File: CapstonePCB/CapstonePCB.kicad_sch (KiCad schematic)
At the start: 30 parts, among them J1 Conn_02x40_Counter_Clockwise, J2 Barrel_Jack, SW1 SW_Push, U1 NUCLEO64-F411RE, U2 LP-MSPM0G3507, U3 STSPIN220, U4 SN74AHC14N, U5 LM7805_TO220, U6 TLV1117-33, U8 APDS-9306

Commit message: Updated routing for PCB
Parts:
- added C2, C3: 0.47 uF, Capacitor_SMD:C_0201_0603Metric, symbol Device:C
- added D2: LED, LED_THT:LED_D3.0mm_FlatTop, symbol Device:LED
- added PullUpResistor2, PullUpResistor3, PullUpResistor4, R2, R3: 10 kOhm, Resistor_SMD:R_0201_0603Metric, symbol Device:R
- added R_STBY2: 5.5k ohm, Resistor_SMD:R_0201_0603Metric, symbol Device:R
- added SW2, SW3: SW_Push, Button_Switch_THT:SW_PUSH_6mm_H7.3mm, symbol Switch:SW_Push
- added U7: COM-09032, Joystick:XDCR_COM-09032, symbol COM-09032:COM-09032
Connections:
- net +12V: now also R_STBY2.1
- net +5V: now also PullUpResistor2.2, PullUpResistor3.2, PullUpResistor4.2
- net GNDREF: now also C1.1, J1.27 (Pin_27), J1.28 (Pin_28), U3.11 (REF), C2.2, C3.2, D2.1 (K), SW2.1, SW3.1, U7.B2A (SEL-), U7.H3 (H-), U7.S1 (SHIELD), U7.S2 (SHIELD), U7.S3 (SHIELD), U7.S4 (SHIELD), U7.V3 (V-); no longer C1.2
- net VDD: now also U7.H1 (H+), U7.V1 (V+)
- net at U3.1 (DIR): now also J1.35 (Pin_35), J1.36 (Pin_36)
- net at U3.15 (MODE2): now also J1.29 (Pin_29), J1.30 (Pin_30)
- net at U3.16 (MODE1): now also J1.31 (Pin_31), J1.32 (Pin_32)
- net at U3.2 (STCK): now also J1.33 (Pin_33), J1.34 (Pin_34)
- net at U3.3 (OUTA1): now also J1.37 (Pin_37), J1.38 (Pin_38)
- net at U3.5 (OUTA2): now also J1.39 (Pin_39), J1.40 (Pin_40)
- net at R1.1, U4.1 (1A): now also C1.2; no longer C1.1
- net at J1.41 (Pin_41), J1.42 (Pin_42): no longer U4.2 (1Y)
- net at U4.3 (2A): now also C2.1, R2.1
- net at U4.4 (2Y): now also J1.3 (Pin_3), J1.4 (Pin_4)
- net at U4.5 (3A): now also C3.1, R3.1
- net at U4.6 (3Y): now also J1.5 (Pin_5), J1.6 (Pin_6)
- net at J1.1 (Pin_1), J1.2 (Pin_2): now also U4.2 (1Y)
- net at J1.21 (Pin_21), J1.22 (Pin_22): now also U7.H2 (H)
- net at J1.23 (Pin_23), J1.24 (Pin_24): now also U7.V2 (V)
- net Button No Debouning: now reaches J1.67 (Pin_67), J1.68 (Pin_68)
- net Button No Debouning: now also PullUpResistor2.1, SW2.2
- net Button Input renamed Button1 Input
- new net: PullUpResistor4.1, R3.2, U7.B1A (SEL+)
- new net: D2.2 (A), R_STBY2.2
- new net Button2 Input: PullUpResistor3.1, R2.2, SW3.2
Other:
- moved on the sheet: C1, C_EN1, C_EN2, C_SPOIL1, C_STBY1, C_s1, D1, J1, PullUpResistor1, R1, R_COFF1, R_COFF2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

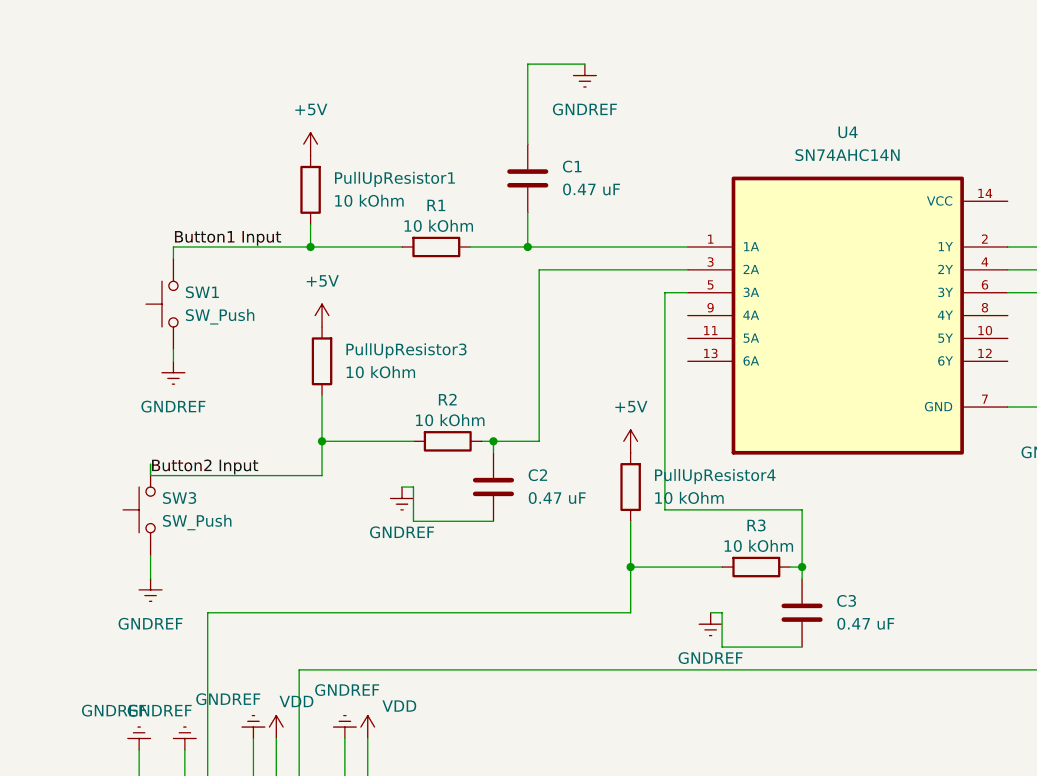
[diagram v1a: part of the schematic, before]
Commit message: Updated button routing
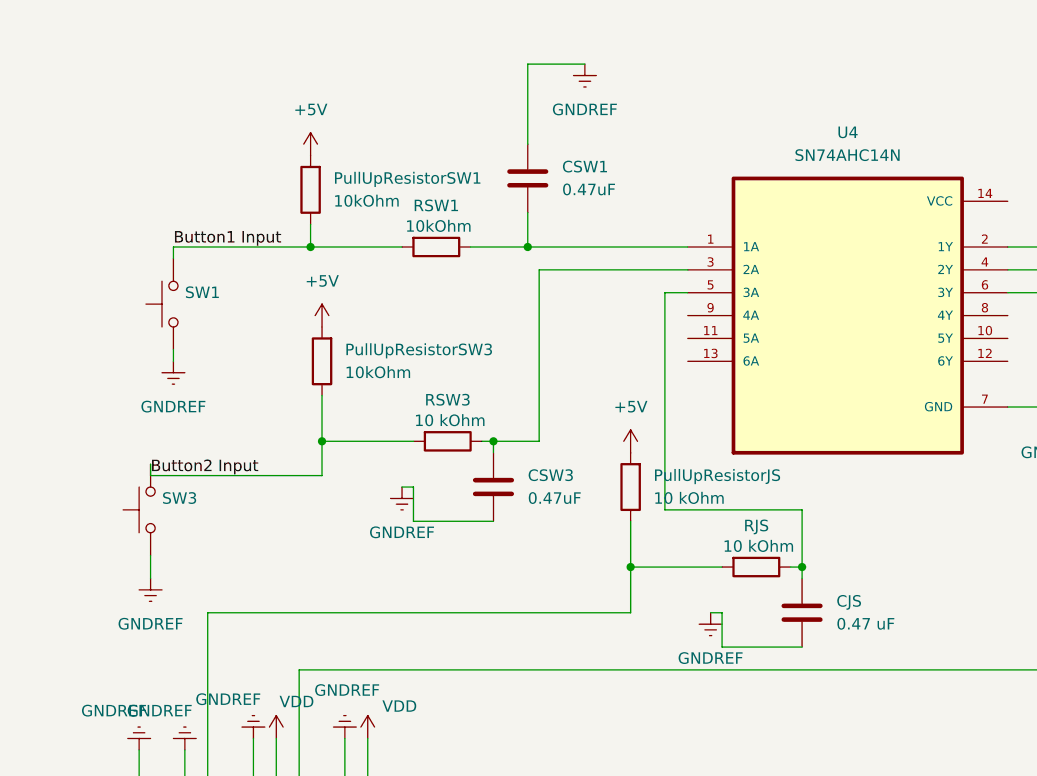
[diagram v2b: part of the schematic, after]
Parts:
- CSW1: renamed from C1; value 0.47 uF -> 0.47uF
- CSW3: renamed from C2; value 0.47 uF -> 0.47uF
- PullUpResistorSW1: renamed from PullUpResistor1; value 10 kOhm -> 10kOhm
- PullUpResistorSW3: renamed from PullUpResistor3; value 10 kOhm -> 10kOhm
- RSW1: renamed from R1; value 10 kOhm -> 10kOhm
- renumbered C3 to CJS, PullUpResistor4 to PullUpResistorJS, R3 to RJS, R2 to RSW3
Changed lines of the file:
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@@
 		(on_board yes)
 		(dnp no)
-		(property "Reference" "R2"
+		(property "Reference" "RSW3"
 			(at 194.31 55.118 90)
 			(effects
@@
 			(project "CapstonePCB"
 				(path "/39e7582f-7765-4fc9-b934-76d5b28d9065"
-					(reference "R2")
+					(reference "RSW3")
 					(unit 1)
 				)
@@
 		(dnp no)
 		(fields_autoplaced yes)
-		(property "Reference" "PullUpResistor1"
+		(property "Reference" "PullUpResistorSW1"
 			(at 181.61 30.4799 0)
 			(effects
@@
 			)
 		)
-		(property "Value" "10 kOhm"
+		(property "Value" "10kOhm"
 			(at 181.61 33.0199 0)
 			(effects
@@
 			(project "CapstonePCB"
 				(path "/39e7582f-7765-4fc9-b934-76d5b28d9065"
-					(reference "PullUpResistor1")
+					(reference "PullUpResistorSW1")
 					(unit 1)
 				)
@@
 		(dnp no)
 		(fields_autoplaced yes)
-		(property "Reference" "C2"
+		(property "Reference" "CSW3"
 			(at 203.2 63.4999 0)
 			(effects
@@
 			)
 		)
-		(property "Value" "0.47 uF"
+		(property "Value" "0.47uF"
 			(at 203.2 66.0399 0)
 			(effects
@@
 			(project "CapstonePCB"
 				(path "/39e7582f-7765-4fc9-b934-76d5b28d9065"
-					(reference "C2")
+					(reference "CSW3")
 					(unit 1)
 				)
@@
 				)
 				(justify right)
+				(hide yes)
 			)
 		)
@@
 		(dnp no)
 		(fields_autoplaced yes)
-		(property "Reference" "C1"
+		(property "Reference" "CSW1"
 			(at 207.01 29.2099 0)
 			(effects
@@
 			)
 		)
-		(property "Value" "0.47 uF"
+		(property "Value" "0.47uF"
 			(at 207.01 31.7499 0)
 			(effects
@@
 			(project ""
 				(path "/39e7582f-7765-4fc9-b934-76d5b28d9065"
-					(reference "C1")
+					(reference "CSW1")
 					(unit 1)
 				)
@@
 		(dnp no)
 		(fields_autoplaced yes)
-		(property "Reference" "PullUpResistor4"
+		(property "Reference" "PullUpResistorJS"
 			(at 217.17 63.4999 0)
 			(effects
@@
 			(project "CapstonePCB"
 				(path "/39e7582f-7765-4fc9-b934-76d5b28d9065"
-					(reference "PullUpResistor4")
+					(reference "PullUpResistorJS")
 					(unit 1)
 				)
@@
 		(on_board yes)
 		(dnp no)
-		(property "Reference" "R3"
+		(property "Reference" "RJS"
 			(at 228.6 69.088 90)
 			(effects
@@
 			(project "CapstonePCB"
 				(path "/39e7582f-7765-4fc9-b934-76d5b28d9065"
-					(reference "R3")
+					(reference "RJS")
 					(unit 1)
 				)
@@
 		(dnp no)
 		(fields_autoplaced yes)
-		(property "Reference" "PullUpResistor3"
+		(property "Reference" "PullUpResistorSW3"
 			(at 182.88 49.5299 0)
 			(effects
@@
 			)
 		)
-		(property "Value" "10 kOhm"
+		(property "Value" "10kOhm"
 			(at 182.88 52.0699 0)
 			(effects
@@
 			(project "CapstonePCB"
 				(path "/39e7582f-7765-4fc9-b934-76d5b28d9065"
-					(reference "PullUpResistor3")
+					(reference "PullUpResistorSW3")
 					(unit 1)
 				)
@@
 		(dnp no)
 		(fields_autoplaced yes)
-		(property "Reference" "C3"
+		(property "Reference" "CJS"
 			(at 237.49 77.4699 0)
 			(effects
@@
 			(project "CapstonePCB"
 				(path "/39e7582f-7765-4fc9-b934-76d5b28d9065"
-					(reference "C3")
+					(reference "CJS")
 					(unit 1)
 				)
@@
 				)
 				(justify right)
+				(hide yes)
 			)
 		)
@@
 		(on_board yes)
 		(dnp no)
-		(property "Reference" "R1"
+		(property "Reference" "RSW1"
 			(at 193.04 33.528 90)
 			(effects
@@
 			)
 		)
-		(property "Value" "10 kOhm"
+		(property "Value" "10kOhm"
 			(at 193.294 35.814 90)
 			(effects
@@
 			(project ""
 				(path "/39e7582f-7765-4fc9-b934-76d5b28d9065"
-					(reference "R1")
+					(reference "RSW1")
 					(unit 1)
 				)

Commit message: Updated naming on silkscreen
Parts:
- renumbered CJS to CJS1, PullUpResistorJS to PullUpResistorJS1, RJS to RJS1
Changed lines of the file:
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@@
 		(dnp no)
 		(fields_autoplaced yes)
-		(property "Reference" "PullUpResistorJS"
+		(property "Reference" "PullUpResistorJS1"
 			(at 217.17 63.4999 0)
 			(effects
@@
 			(project "CapstonePCB"
 				(path "/39e7582f-7765-4fc9-b934-76d5b28d9065"
-					(reference "PullUpResistorJS")
+					(reference "PullUpResistorJS1")
 					(unit 1)
 				)
@@
 		(on_board yes)
 		(dnp no)
-		(property "Reference" "RJS"
+		(property "Reference" "RJS1"
 			(at 228.6 69.088 90)
 			(effects
@@
 			(project "CapstonePCB"
 				(path "/39e7582f-7765-4fc9-b934-76d5b28d9065"
-					(reference "RJS")
+					(reference "RJS1")
 					(unit 1)
 				)
@@
 		(dnp no)
 		(fields_autoplaced yes)
-		(property "Reference" "CJS"
+		(property "Reference" "CJS1"
 			(at 237.49 77.4699 0)
 			(effects
@@
 			(project "CapstonePCB"
 				(path "/39e7582f-7765-4fc9-b934-76d5b28d9065"
-					(reference "CJS")
-					(unit 1)
-				)
+					(reference "CJS1")
+					(unit 1)
+				)

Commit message: Updated rounting
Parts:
- renumbered C_STBY2 to C_BP1, C_STBY3 to C_BP2, R_STBY2 to R_INDC
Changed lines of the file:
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@@
 		(dnp no)
 		(fields_autoplaced yes)
-		(property "Reference" "R_STBY2"
+		(property "Reference" "R_INDC"
 			(at 31.75 177.7999 0)
 			(effects
@@
 			(project "CapstonePCB"
 				(path "/39e7582f-7765-4fc9-b934-76d5b28d9065"
-					(reference "R_STBY2")
+					(reference "R_INDC")
 					(unit 1)
 				)
@@
 		(dnp no)
 		(fields_autoplaced yes)
-		(property "Reference" "C_STBY3"
+		(property "Reference" "C_BP2"
 			(at 54.61 21.5962 0)
 			(effects
@@
 			(project "CapstonePCB"
 				(path "/39e7582f-7765-4fc9-b934-76d5b28d9065"
-					(reference "C_STBY3")
+					(reference "C_BP2")
 					(unit 1)
 				)
@@
 		(dnp no)
 		(fields_autoplaced yes)
-		(property "Reference" "C_STBY2"
+		(property "Reference" "C_BP1"
 			(at 41.91 21.5962 0)
 			(effects
@@
 			(project "CapstonePCB"
 				(path "/39e7582f-7765-4fc9-b934-76d5b28d9065"
-					(reference "C_STBY2")
+					(reference "C_BP1")
 					(unit 1)
 				)

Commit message: Formatting change
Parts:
- renumbered R_INDC to R_INDC1
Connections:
- net GNDREF: no longer J1.27 (Pin_27), J1.28 (Pin_28), U3.11 (REF)
- net at J1.21 (Pin_21), J1.22 (Pin_22): no longer U7.H2 (H)
- net at J1.23 (Pin_23), J1.24 (Pin_24): no longer U7.V2 (V)
- net at J1.11 (Pin_11), J1.12 (Pin_12): now also U7.H2 (H)
- net at J1.13 (Pin_13), J1.14 (Pin_14): now also U7.V2 (V)
- new net: J1.27 (Pin_27), J1.28 (Pin_28), U3.11 (REF)

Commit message: Changed caps to through-hole
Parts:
- C_EN1, C_EN2, C_SPOIL1, C_STBY1, C_s1: footprint Capacitor_SMD:C_0201_0603Metric -> Capacitor_THT:C_Disc_D4.3mm_W1.9mm_P5.00mm
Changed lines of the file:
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@@
 			)
 		)
-		(property "Footprint" "Capacitor_SMD:C_0201_0603Metric"
+		(property "Footprint" "Capacitor_THT:C_Disc_D4.3mm_W1.9mm_P5.00mm"
 			(at 306.07 147.32 0)
 			(effects
@@
 			)
 		)
-		(property "Footprint" "Capacitor_SMD:C_0201_0603Metric"
+		(property "Footprint" "Capacitor_THT:C_Disc_D4.3mm_W1.9mm_P5.00mm"
 			(at 241.3 203.2 0)
 			(effects
@@
 			)
 		)
-		(property "Footprint" "Capacitor_SMD:C_0201_0603Metric"
+		(property "Footprint" "Capacitor_THT:C_Disc_D4.3mm_W1.9mm_P5.00mm"
 			(at 233.68 179.07 0)
 			(effects
@@
 			)
 		)
-		(property "Footprint" "Capacitor_SMD:C_0201_0603Metric"
+		(property "Footprint" "Capacitor_THT:C_Disc_D4.3mm_W1.9mm_P5.00mm"
 			(at 284.48 147.32 0)
 			(effects
@@
 			)
 		)
-		(property "Footprint" "Capacitor_SMD:C_0201_0603Metric"
+		(property "Footprint" "Capacitor_THT:C_Disc_D4.3mm_W1.9mm_P5.00mm"
 			(at 218.44 176.53 0)
 			(effects

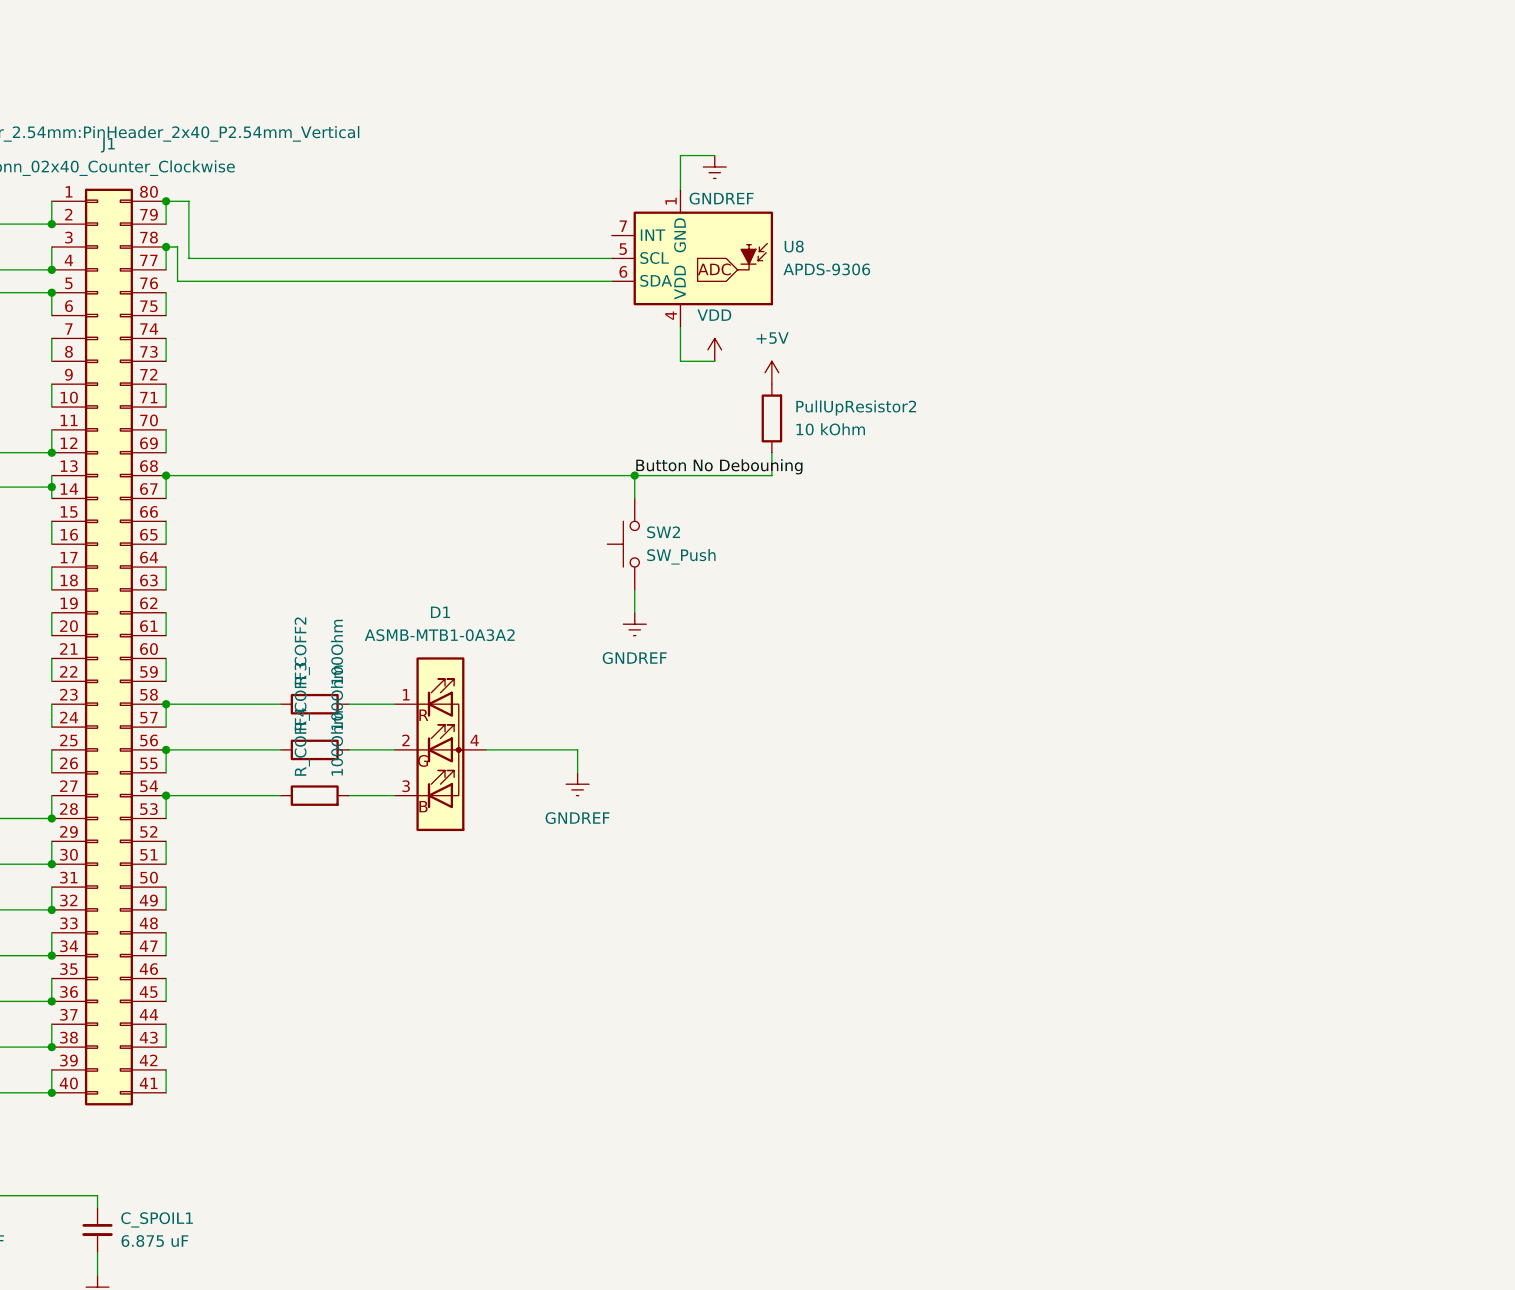
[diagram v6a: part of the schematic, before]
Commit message: Added LCD connector to schematic
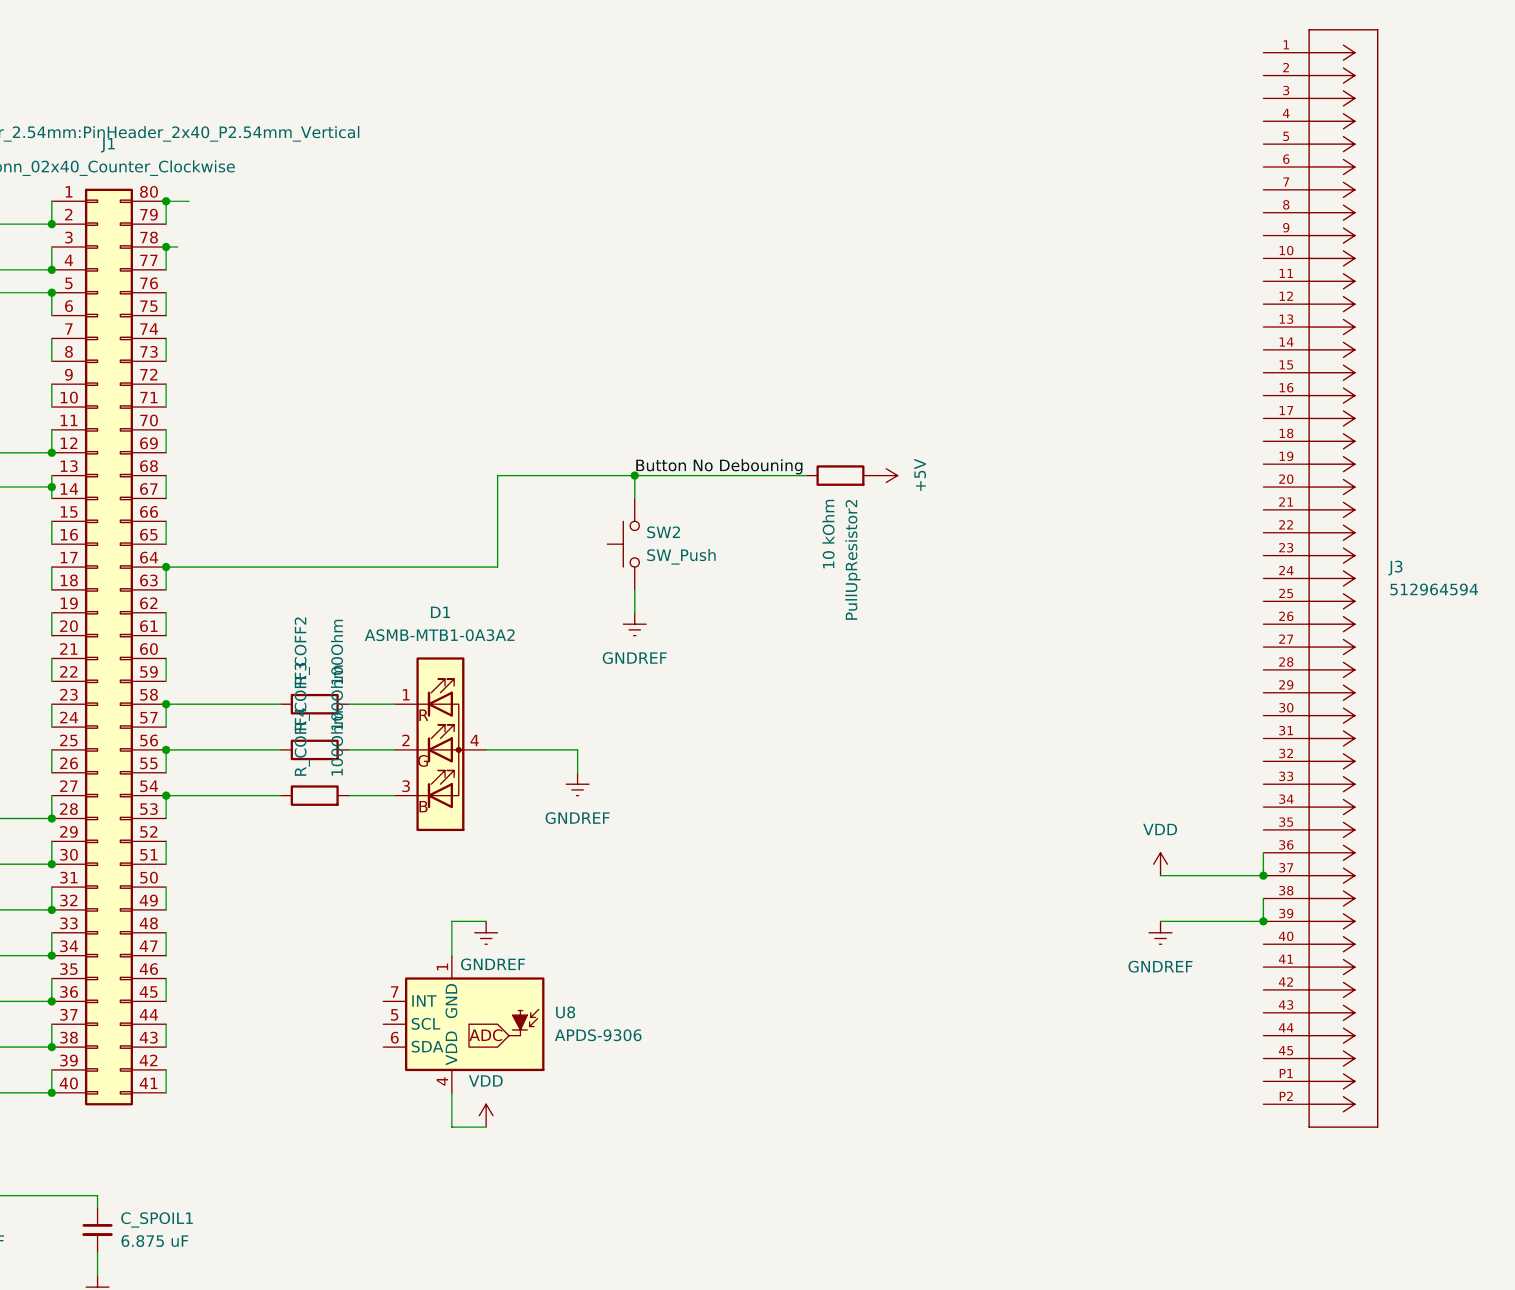
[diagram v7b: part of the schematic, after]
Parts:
- added J3: 512964594, CorrectlLCDconnector:CON_512964594_MOL, symbol 512964594:512964594
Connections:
- net Button No Debouning: now also J1.63 (Pin_63), J1.64 (Pin_64); no longer J1.67 (Pin_67), J1.68 (Pin_68)
- net GNDREF: now also J3.38, J3.39
- net VDD: now also J3.36, J3.37
- net at J1.79 (Pin_79), J1.80 (Pin_80): no longer U8.5 (SCL)
- net at J1.77 (Pin_77), J1.78 (Pin_78): no longer U8.6 (SDA)
- new net: J1.67 (Pin_67), J1.68 (Pin_68)
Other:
- moved on the sheet: PullUpResistor2, U8
